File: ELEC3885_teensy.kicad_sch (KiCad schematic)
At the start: 1 part, among them U3 Teensy4.1

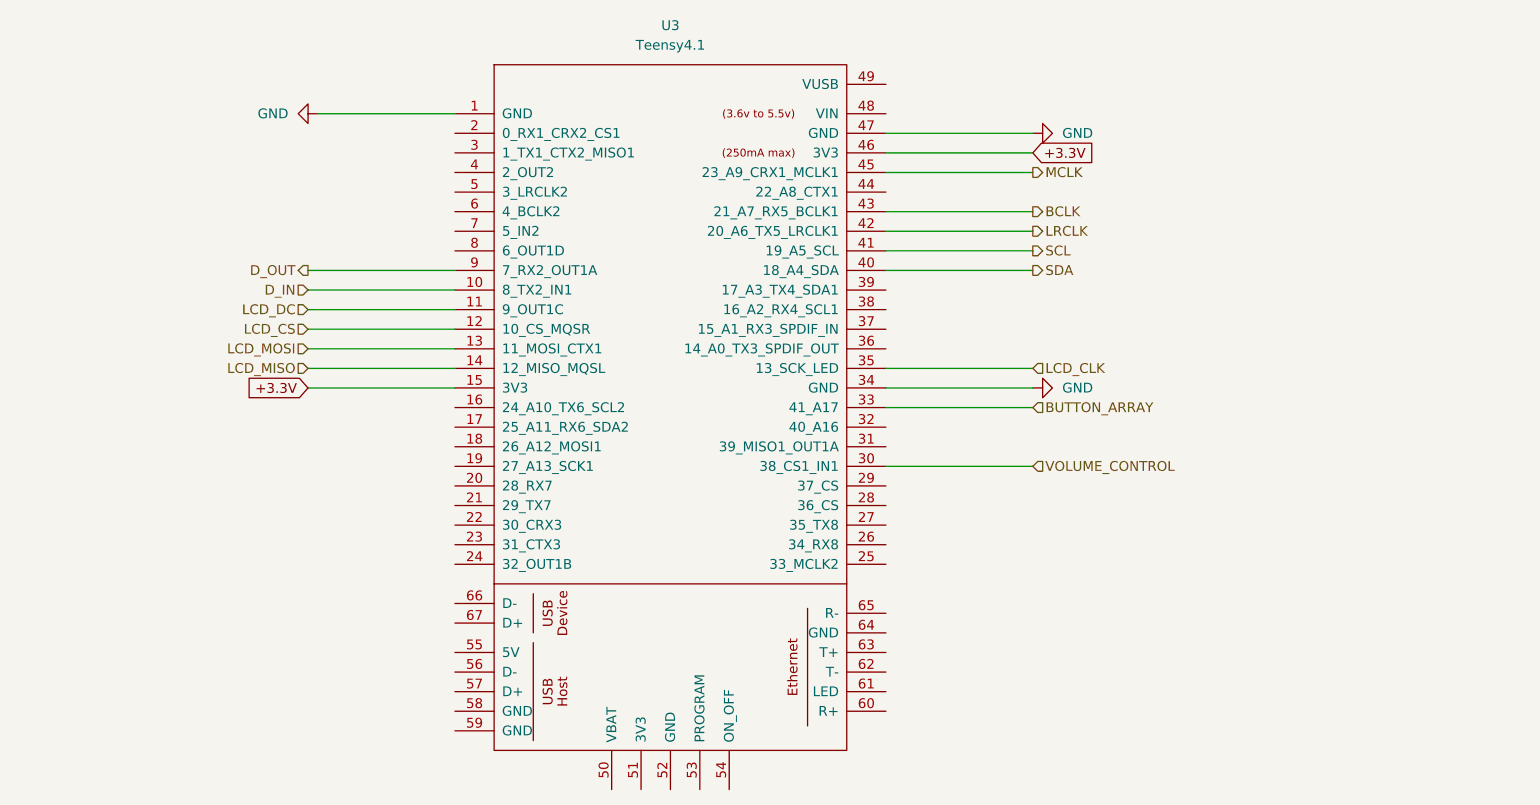
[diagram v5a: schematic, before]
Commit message: Rev3 rework, diff amp jumpers added
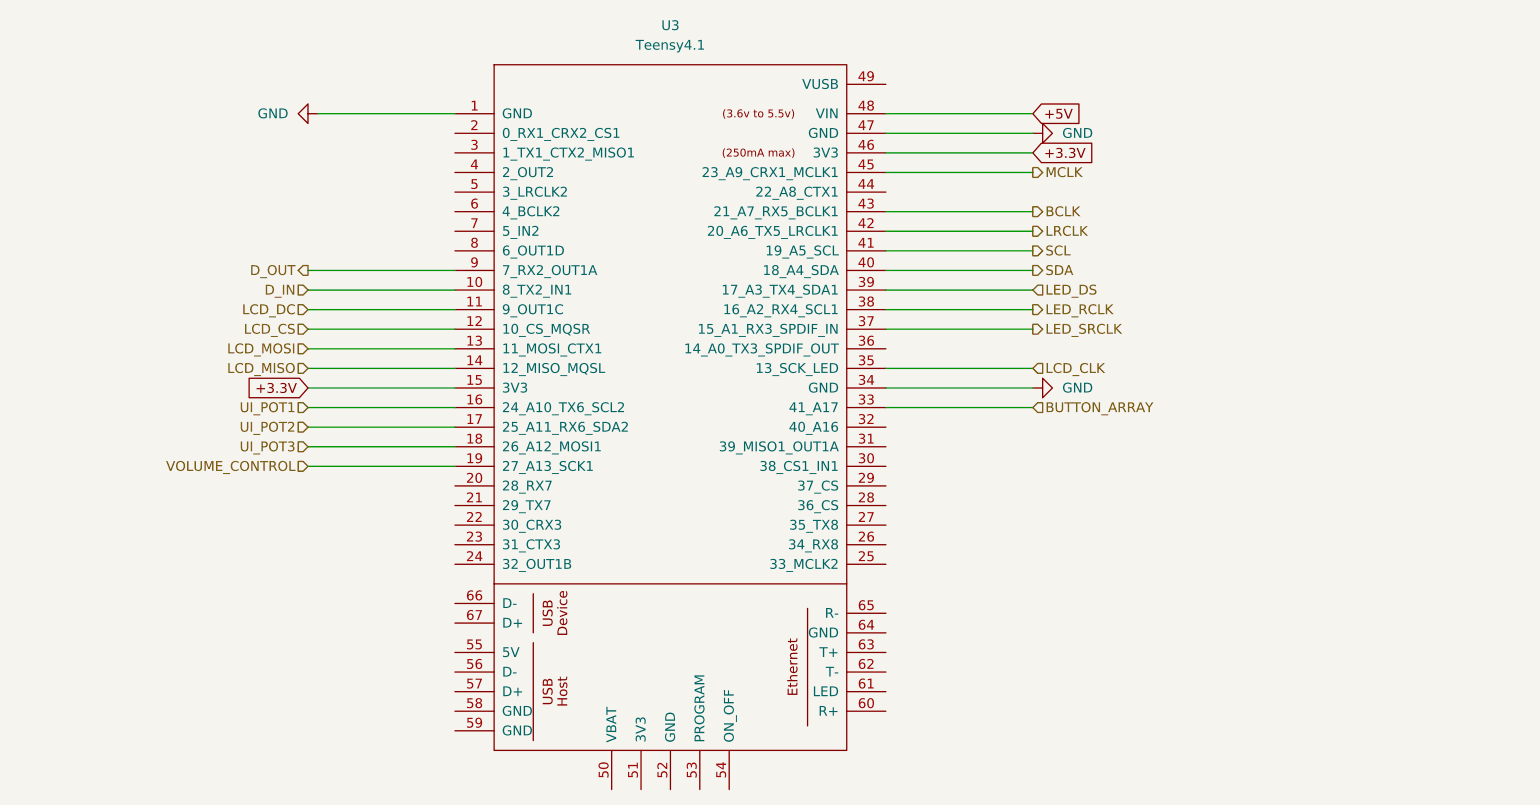
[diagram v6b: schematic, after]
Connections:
- net VOLUME_CONTROL: now also U3.19 (27_A13_SCK1); no longer U3.30 (38_CS1_IN1)
- net UI_POT1: now reaches U3.16 (24_A10_TX6_SCL2)
- net UI_POT2: now reaches U3.17 (25_A11_RX6_SDA2)
- net UI_POT3: now reaches U3.18 (26_A12_MOSI1)
- net LED_SRCLK: now reaches U3.37 (15_A1_RX3_SPDIF_IN)
- net LED_RCLK: now reaches U3.38 (16_A2_RX4_SCL1)
- net LED_DS: now reaches U3.39 (17_A3_TX4_SDA1)
- net +5V: now reaches U3.48 (VIN)
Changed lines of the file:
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@@
-    (stroke (width 0) (type default))
-  )
-  (wire (pts (xy 143.51 96.52) (xy 162.56 96.52))
     (stroke (width 0) (type default))
   )
@@
     (stroke (width 0) (type default))
   )
+  (wire (pts (xy 162.56 76.2) (xy 143.51 76.2))
+    (stroke (width 0) (type default))
+  )
   (wire (pts (xy 143.51 55.88) (xy 162.56 55.88))
     (stroke (width 0) (type default))
   )
+  (wire (pts (xy 162.56 50.8) (xy 143.51 50.8))
+    (stroke (width 0) (type default))
+  )
   (wire (pts (xy 68.58 83.82) (xy 87.63 83.82))
+    (stroke (width 0) (type default))
+  )
+  (wire (pts (xy 68.58 88.9) (xy 87.63 88.9))
     (stroke (width 0) (type default))
   )
@@
     (stroke (width 0) (type default))
   )
+  (wire (pts (xy 68.58 93.98) (xy 87.63 93.98))
+    (stroke (width 0) (type default))
+  )
   (wire (pts (xy 143.51 53.34) (xy 162.56 53.34))
     (stroke (width 0) (type default))
@@
     (stroke (width 0) (type default))
   )
+  (wire (pts (xy 68.58 96.52) (xy 87.63 96.52))
+    (stroke (width 0) (type default))
+  )
   (wire (pts (xy 162.56 83.82) (xy 143.51 83.82))
     (stroke (width 0) (type default))
   )
   (wire (pts (xy 68.58 76.2) (xy 87.63 76.2))
+    (stroke (width 0) (type default))
+  )
+  (wire (pts (xy 162.56 73.66) (xy 143.51 73.66))
+    (stroke (width 0) (type default))
+  )
+  (wire (pts (xy 162.56 78.74) (xy 143.51 78.74))
     (stroke (width 0) (type default))
   )
@@
     (stroke (width 0) (type default))
   )
+  (wire (pts (xy 68.58 91.44) (xy 87.63 91.44))
+    (stroke (width 0) (type default))
+  )
+  (global_label "+5V" (shape input) (at 162.56 50.8 0) (fields_autoplaced)
+    (effects (font (size 1.27 1.27)) (justify left))
+    (property "Intersheetrefs" "${INTERSHEET_REFS}" (at 169.3363 50.8 0)
+      (effects (font (size 1.27 1.27)) (justify left) hide)
+    )
+  )
   (global_label "+3.3V" (shape input) (at 68.58 86.36 180) (fields_autoplaced)
     (effects (font (size 1.27 1.27)) (justify right))
@@
     )
   )
+  (hierarchical_label "UI_POT3" (shape input) (at 68.58 93.98 180) (fields_autoplaced)
+    (effects (font (size 1.27 1.27)) (justify right))
+  )
+  (hierarchical_label "LED_RCLK" (shape output) (at 162.56 76.2 0) (fields_autoplaced)
+    (effects (font (size 1.27 1.27)) (justify left))
+  )
   (hierarchical_label "D_IN" (shape input) (at 68.58 73.66 180) (fields_autoplaced)
     (effects (font (size 1.27 1.27)) (justify right))
@@
     (effects (font (size 1.27 1.27)) (justify right))
   )
-  (hierarchical_label "VOLUME_CONTROL" (shape input) (at 162.56 96.52 0) (fields_autoplaced)
-    (effects (font (size 1.27 1.27)) (justify left))
+  (hierarchical_label "VOLUME_CONTROL" (shape input) (at 68.58 96.52 180) (fields_autoplaced)
+    (effects (font (size 1.27 1.27)) (justify right))
   )
   (hierarchical_label "SDA" (shape output) (at 162.56 71.12 0) (fields_autoplaced)
@@
     (effects (font (size 1.27 1.27)) (justify left))
   )
+  (hierarchical_label "LED_DS" (shape input) (at 162.56 73.66 0) (fields_autoplaced)
+    (effects (font (size 1.27 1.27)) (justify left))
+  )
   (hierarchical_label "D_OUT" (shape output) (at 68.58 71.12 180) (fields_autoplaced)
     (effects (font (size 1.27 1.27)) (justify right))
@@
   (hierarchical_label "BUTTON_ARRAY" (shape input) (at 162.56 88.9 0) (fields_autoplaced)
     (effects (font (size 1.27 1.27)) (justify left))
+  )
+  (hierarchical_label "UI_POT1" (shape input) (at 68.58 88.9 180) (fields_autoplaced)
+    (effects (font (size 1.27 1.27)) (justify right))
   )
   (hierarchical_label "LCD_MOSI" (shape input) (at 68.58 81.28 180) (fields_autoplaced)
@@
     (effects (font (size 1.27 1.27)) (justify left))
   )
+  (hierarchical_label "LED_SRCLK" (shape output) (at 162.56 78.74 0) (fields_autoplaced)
+    (effects (font (size 1.27 1.27)) (justify left))
+  )
+  (hierarchical_label "UI_POT2" (shape input) (at 68.58 91.44 180) (fields_autoplaced)
+    (effects (font (size 1.27 1.27)) (justify right))
+  )
   (hierarchical_label "SCL" (shape output) (at 162.56 68.58 0) (fields_autoplaced)

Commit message: Encoders, RGB LED added, PCB cleanup
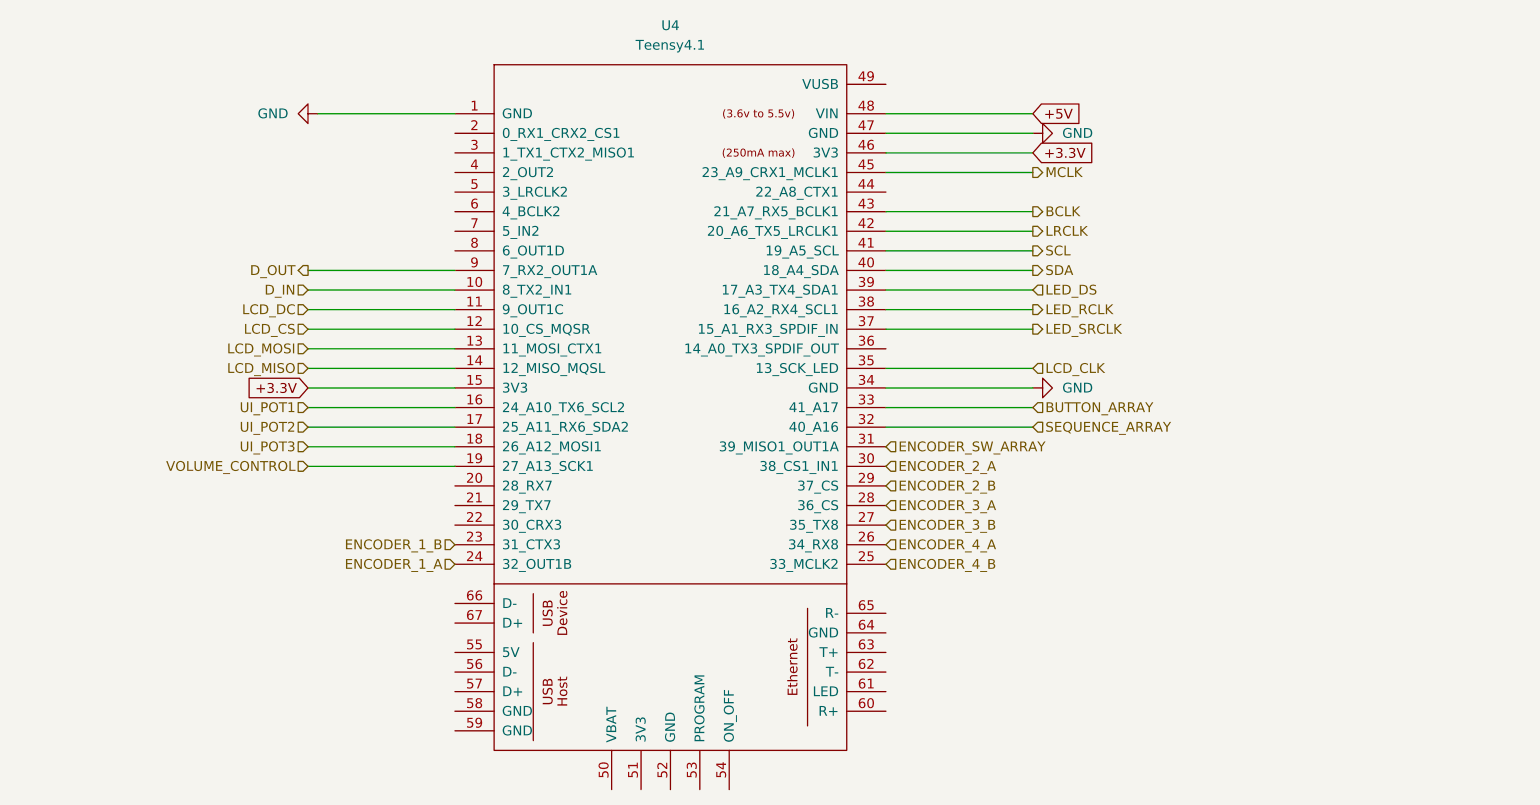
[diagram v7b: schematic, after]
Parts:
- renumbered U3 to U4
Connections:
- net ENCODER_1_B: now reaches U4.23 (31_CTX3)
- net ENCODER_1_A: now reaches U4.24 (32_OUT1B)
- net ENCODER_4_B: now reaches U4.25 (33_MCLK2)
- net ENCODER_4_A: now reaches U4.26 (34_RX8)
- net ENCODER_3_B: now reaches U4.27 (35_TX8)
- net ENCODER_3_A: now reaches U4.28 (36_CS)
- net ENCODER_2_B: now reaches U4.29 (37_CS)
- net ENCODER_2_A: now reaches U4.30 (38_CS1_IN1)
- net ENCODER_SW_ARRAY: now reaches U4.31 (39_MISO1_OUT1A)
- net SEQUENCE_ARRAY: now reaches U4.32 (40_A16)
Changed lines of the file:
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@@
+    (stroke (width 0) (type default))
+  )
+  (wire (pts (xy 143.51 91.44) (xy 162.56 91.44))
     (stroke (width 0) (type default))
   )
@@
     (effects (font (size 1.27 1.27)) (justify left))
   )
+  (hierarchical_label "ENCODER_3_A" (shape input) (at 143.51 101.6 0) (fields_autoplaced)
+    (effects (font (size 1.27 1.27)) (justify left))
+  )
   (hierarchical_label "LCD_DC" (shape input) (at 68.58 76.2 180) (fields_autoplaced)
     (effects (font (size 1.27 1.27)) (justify right))
@@
     (effects (font (size 1.27 1.27)) (justify left))
   )
+  (hierarchical_label "ENCODER_4_A" (shape input) (at 143.51 106.68 0) (fields_autoplaced)
+    (effects (font (size 1.27 1.27)) (justify left))
+  )
   (hierarchical_label "LCD_MISO" (shape input) (at 68.58 83.82 180) (fields_autoplaced)
     (effects (font (size 1.27 1.27)) (justify right))
@@
     (effects (font (size 1.27 1.27)) (justify right))
   )
+  (hierarchical_label "SEQUENCE_ARRAY" (shape input) (at 162.56 91.44 0) (fields_autoplaced)
+    (effects (font (size 1.27 1.27)) (justify left))
+  )
   (hierarchical_label "BUTTON_ARRAY" (shape input) (at 162.56 88.9 0) (fields_autoplaced)
     (effects (font (size 1.27 1.27)) (justify left))
@@
     (effects (font (size 1.27 1.27)) (justify right))
   )
+  (hierarchical_label "ENCODER_1_B" (shape input) (at 87.63 106.68 180) (fields_autoplaced)
+    (effects (font (size 1.27 1.27)) (justify right))
+  )
   (hierarchical_label "LCD_MOSI" (shape input) (at 68.58 81.28 180) (fields_autoplaced)
     (effects (font (size 1.27 1.27)) (justify right))
   )
+  (hierarchical_label "ENCODER_2_A" (shape input) (at 143.51 96.52 0) (fields_autoplaced)
+    (effects (font (size 1.27 1.27)) (justify left))
+  )
   (hierarchical_label "LRCLK" (shape output) (at 162.56 66.04 0) (fields_autoplaced)
     (effects (font (size 1.27 1.27)) (justify left))
@@
     (effects (font (size 1.27 1.27)) (justify left))
   )
+  (hierarchical_label "ENCODER_3_B" (shape input) (at 143.51 104.14 0) (fields_autoplaced)
+    (effects (font (size 1.27 1.27)) (justify left))
+  )
+  (hierarchical_label "ENCODER_1_A" (shape input) (at 87.63 109.22 180) (fields_autoplaced)
+    (effects (font (size 1.27 1.27)) (justify right))
+  )
   (hierarchical_label "UI_POT2" (shape input) (at 68.58 91.44 180) (fields_autoplaced)
     (effects (font (size 1.27 1.27)) (justify right))
   )
+  (hierarchical_label "ENCODER_4_B" (shape input) (at 143.51 109.22 0) (fields_autoplaced)
+    (effects (font (size 1.27 1.27)) (justify left))
+  )
   (hierarchical_label "SCL" (shape output) (at 162.56 68.58 0) (fields_autoplaced)
     (effects (font (size 1.27 1.27)) (justify left))
   )
+  (hierarchical_label "ENCODER_2_B" (shape input) (at 143.51 99.06 0) (fields_autoplaced)
+    (effects (font (size 1.27 1.27)) (justify left))
+  )
+  (hierarchical_label "ENCODER_SW_ARRAY" (shape input) (at 143.51 93.98 0) (fields_autoplaced)
+    (effects (font (size 1.27 1.27)) (justify left))
+  )
   (symbol (lib_id "power:GND") (at 162.56 53.34 90) (unit 1)
     (in_bom yes) (on_board yes) (dnp no) (fields_autoplaced)
-    (property "Reference" "#PWR016" (at 168.91 53.34 0)
+    (property "Reference" "#PWR019" (at 168.91 53.34 0)
       (effects (font (size 1.27 1.27)) hide)
     )
@@
       (project "ELEC3885"
         (path "/eaef1172-3351-417c-bfc4-74a598f141cb/3c9f2675-bcfe-4a13-8988-99caeafacad4"
-          (reference "#PWR016") (unit 1)
+          (reference "#PWR019") (unit 1)
         )
       )
@@
   (symbol (lib_id "power:GND") (at 69.85 50.8 270) (unit 1)
     (in_bom yes) (on_board yes) (dnp no) (fields_autoplaced)
-    (property "Reference" "#PWR015" (at 63.5 50.8 0)
+    (property "Reference" "#PWR018" (at 63.5 50.8 0)
       (effects (font (size 1.27 1.27)) hide)
     )
@@
       (project "ELEC3885"
         (path "/eaef1172-3351-417c-bfc4-74a598f141cb/3c9f2675-bcfe-4a13-8988-99caeafacad4"
-          (reference "#PWR015") (unit 1)
+          (reference "#PWR018") (unit 1)
         )
       )
@@
   (symbol (lib_id "teensy:Teensy4.1") (at 115.57 105.41 0) (unit 1)
     (in_bom yes) (on_board yes) (dnp no) (fields_autoplaced)
-    (property "Reference" "U3" (at 115.57 39.37 0)
+    (property "Reference" "U4" (at 115.57 39.37 0)
       (effects (font (size 1.27 1.27)))
     )
@@
       (project "ELEC3885"
         (path "/eaef1172-3351-417c-bfc4-74a598f141cb/3c9f2675-bcfe-4a13-8988-99caeafacad4"
-          (reference "U3") (unit 1)
+          (reference "U4") (unit 1)
         )
       )
@@
   (symbol (lib_id "power:GND") (at 162.56 86.36 90) (unit 1)
     (in_bom yes) (on_board yes) (dnp no) (fields_autoplaced)
-    (property "Reference" "#PWR017" (at 168.91 86.36 0)
+    (property "Reference" "#PWR020" (at 168.91 86.36 0)
       (effects (font (size 1.27 1.27)) hide)
     )
@@
       (project "ELEC3885"
         (path "/eaef1172-3351-417c-bfc4-74a598f141cb/3c9f2675-bcfe-4a13-8988-99caeafacad4"
-          (reference "#PWR017") (unit 1)
-        )
-      )
+          (reference "#PWR020") (unit 1)
+        )
+      )

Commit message: LED foorprint fix, ground planes fix
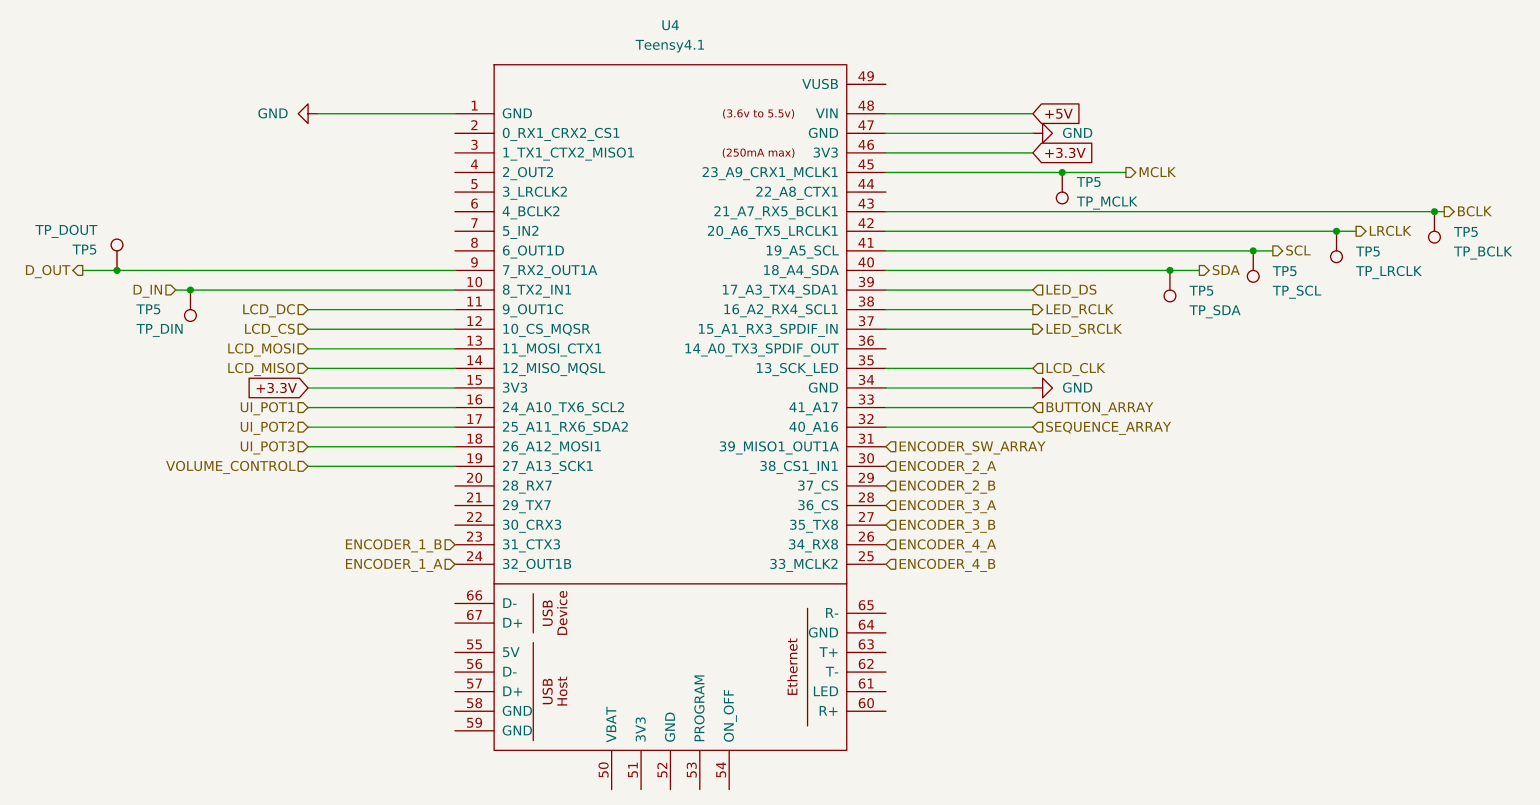
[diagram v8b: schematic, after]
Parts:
- added TP5: TP_LRCLK, TestPoint:TestPoint_Pad_D1.0mm, symbol Connector:TestPoint
- added TP5: TP_SCL, TestPoint:TestPoint_Pad_D1.0mm, symbol Connector:TestPoint
- added TP5: TP_BCLK, TestPoint:TestPoint_Pad_D1.0mm, symbol Connector:TestPoint
- added TP5: TP_DIN, TestPoint:TestPoint_Pad_D1.0mm, symbol Connector:TestPoint
- added TP5: TP_DOUT, TestPoint:TestPoint_Pad_D1.0mm, symbol Connector:TestPoint
- added TP5: TP_SDA, TestPoint:TestPoint_Pad_D1.0mm, symbol Connector:TestPoint
- added TP5: TP_MCLK, TestPoint:TestPoint_Pad_D1.0mm, symbol Connector:TestPoint
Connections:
- net BCLK: now also TP5.1
- net D_IN: now also TP5.1
- net D_OUT: now also TP5.1
- net LRCLK: now also TP5.1
- net MCLK: now also TP5.1
- net SCL: now also TP5.1
- net SDA: now also TP5.1
